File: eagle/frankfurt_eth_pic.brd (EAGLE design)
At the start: 72.2 x 65.5 mm, 62 parts, among them IC1 PIC18F26K80, IC2 ENC28J60-SO, IC3 SN65HVD232, IC4 LM2575S, IC5 11AA02E48, IC6 MCP23A256, IC7 AT45DB041D, J2 A00-108-220-450, Q1 10 MHz, Q2 25 MHz

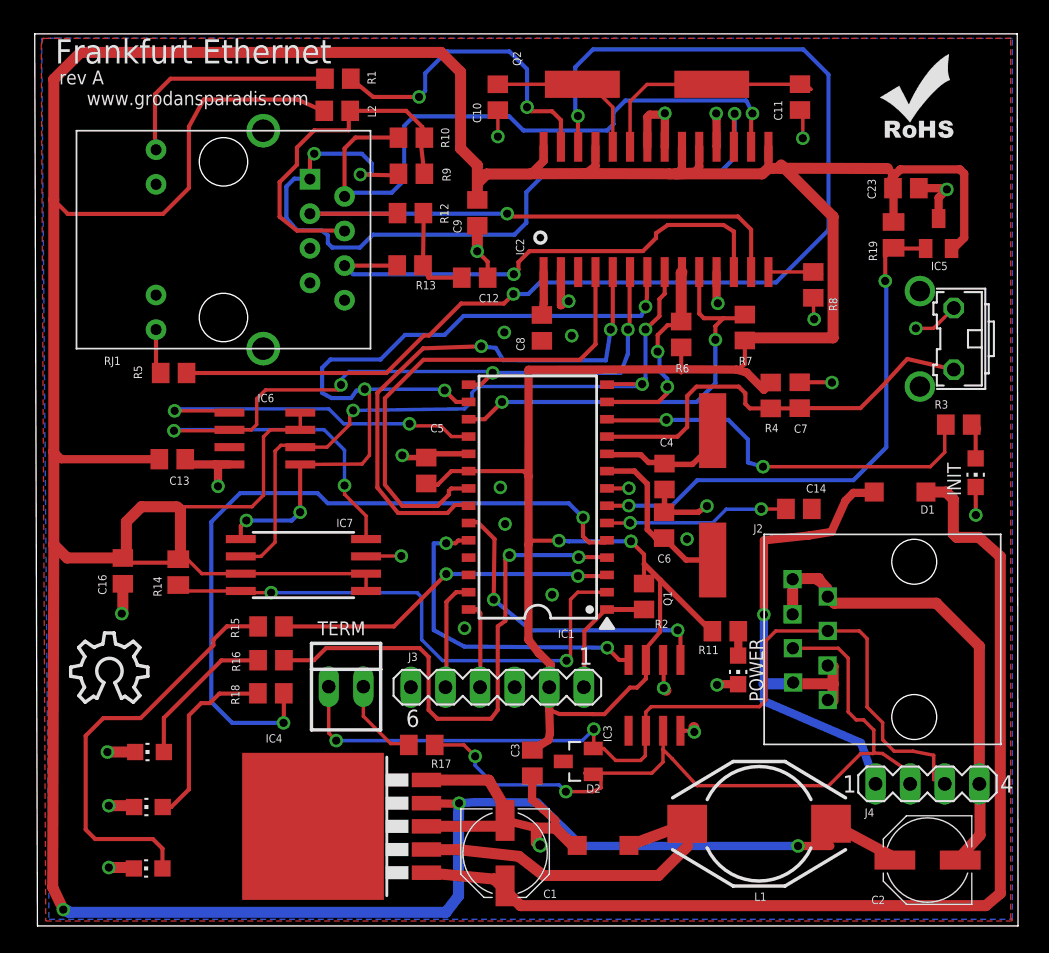
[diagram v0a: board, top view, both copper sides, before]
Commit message: Changed layer for info text on pic board
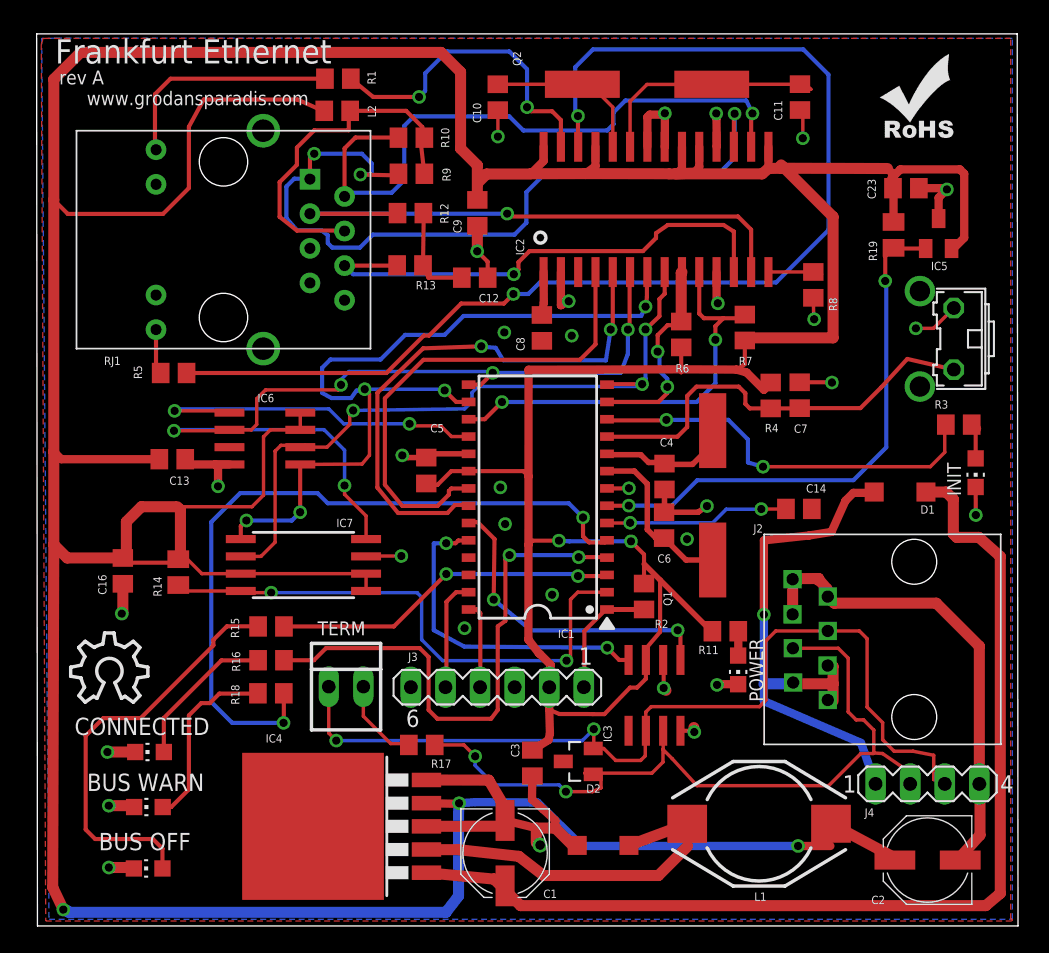
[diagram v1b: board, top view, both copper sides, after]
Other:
- board size 72.2 x 65.5 mm -> 72.1 x 65.5 mm
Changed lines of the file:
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@@
 <text x="53.29" y="16.46" size="1.016" layer="25" font="fixed" rot="R90">POWER</text>
 <text x="67.81" y="31.57" size="1.016" layer="25" font="fixed" rot="R90">INIT</text>
-<wire x1="0" y1="0" x2="-0.2" y2="65.5" width="0" layer="20"/>
-<wire x1="-0.2" y1="65.5" x2="71.94" y2="65.5" width="0" layer="20"/>
+<wire x1="0" y1="0" x2="-0.06" y2="65.5" width="0" layer="20"/>
+<wire x1="-0.06" y1="65.5" x2="71.94" y2="65.5" width="0" layer="20"/>
 <wire x1="71.94" y1="65.5" x2="72" y2="0" width="0" layer="20"/>
 <wire x1="72" y1="0" x2="0" y2="0" width="0" layer="20"/>
 <circle x="36.93" y="50.54" radius="0.1220625" width="0.8128" layer="25"/>
-<text x="2.72" y="14.02" size="1.27" layer="51">CONNECTED</text>
-<text x="3.64" y="9.91" size="1.27" layer="51">BUS WARN</text>
-<text x="4.5" y="5.56" size="1.27" layer="51">BUS OFF</text>
+<text x="2.72" y="14.02" size="1.27" layer="25">CONNECTED</text>
+<text x="3.64" y="9.91" size="1.27" layer="25">BUS WARN</text>
+<text x="4.5" y="5.56" size="1.27" layer="25">BUS OFF</text>
 </plain>
 <attributes>
